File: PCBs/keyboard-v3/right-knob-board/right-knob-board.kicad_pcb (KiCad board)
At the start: 2 copper layers, 58 x 59 mm, 36 parts, among them J101 F31L-1A7H1-11008, M1 2206-100T, Q101 DMP21D0UFB-7B, Q102 DMP21D0UFB-7B, Q201 DMN21D2UFB-7B, SW1 SW_DIP_x01, SW2 SW_DIP_x01, SW3 SW_DIP_x01, U101 TMC6300-LA, U102 AS5600, U103 STM32U031C6Ux

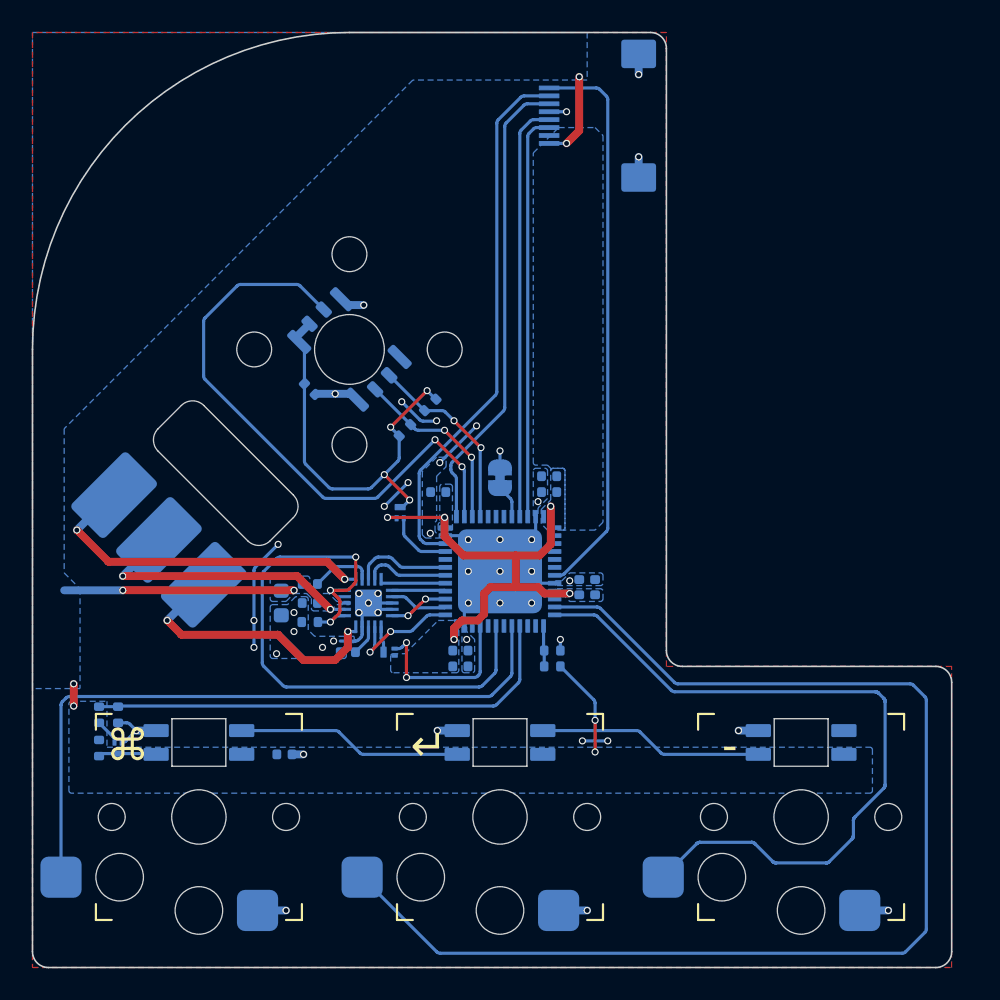
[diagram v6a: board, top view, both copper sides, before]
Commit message: Added mounting holes
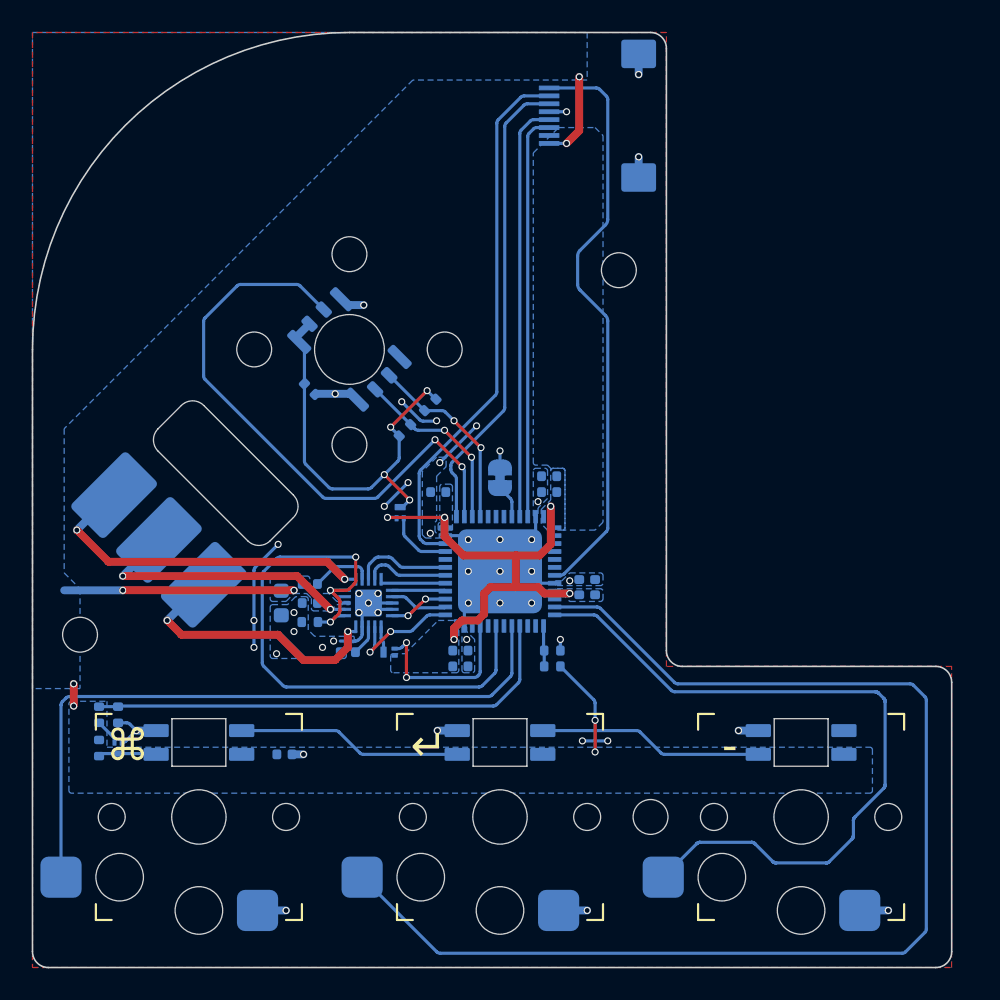
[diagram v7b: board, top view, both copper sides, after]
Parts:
- added H1: MountingHole, MountingHole:MountingHole_2.2mm_M2, F.Cu at (155.0, 75.0)
- added H2: MountingHole, MountingHole:MountingHole_2.2mm_M2, F.Cu at (121.0, 98.0)
- added H3: MountingHole, MountingHole:MountingHole_2.2mm_M2, F.Cu at (157.0, 109.5)
- renumbered C201 to C1, C106 to C10, C107 to C11, C3 to C12, C105 to C13, C109 to C2, C103 to C3, C102 to C4, C101 to C5, C104 to C6, C108 to C7, C1 to C8, C2 to C9, J101 to J1, JP101 to JP1, Q102 to Q1, Q201 to Q2, Q101 to Q3, R201 to R1, R104 to R2, R105 to R3, R202 to R4, R203 to R5, R106 to R6, R107 to R7, R101 to R8, U102 to U1, U101 to U2, U103 to U3
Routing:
- net /~{RST}: track 35.7 -> 37.2 mm

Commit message: Left key board done
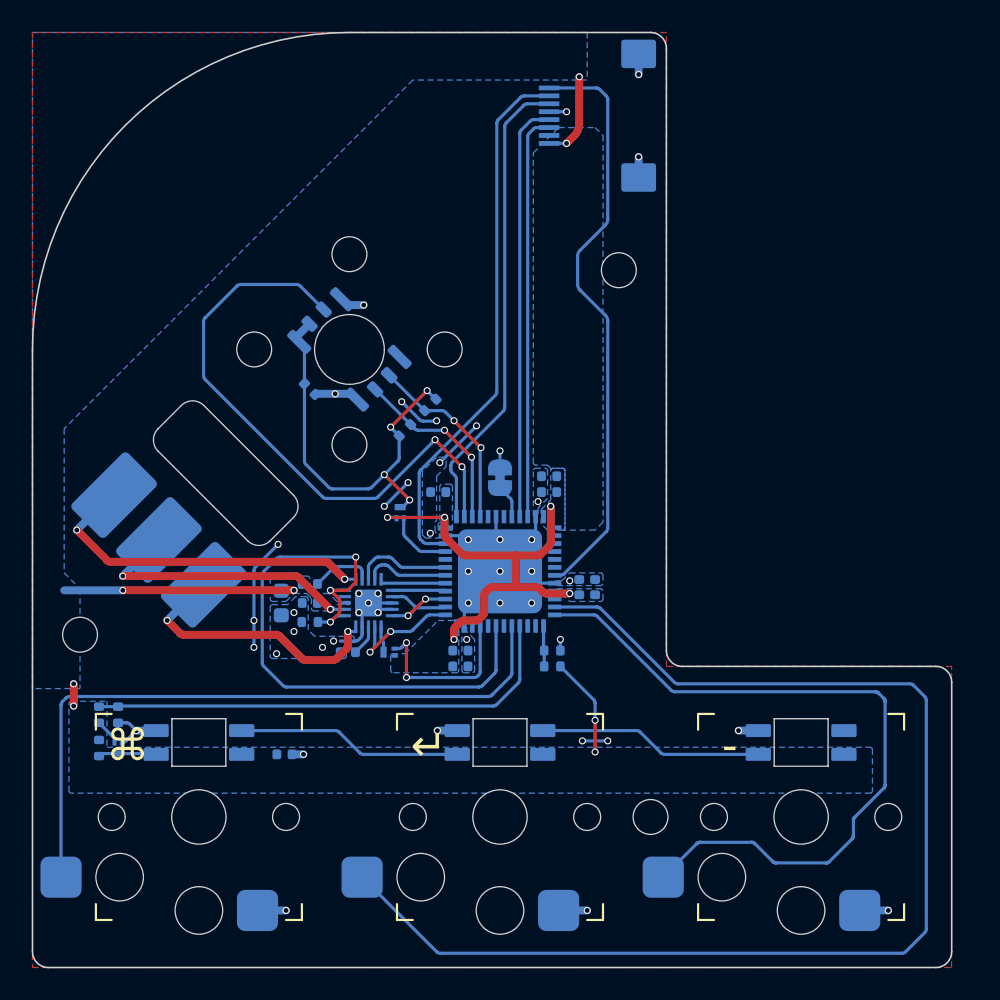
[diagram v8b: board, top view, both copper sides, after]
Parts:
- H3: moved to B.Cu
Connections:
- U3 pad 42: unconnected-(U3-PB6-Pad42) -> GND
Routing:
- net GND: track 62.7 -> 66.3 mm
